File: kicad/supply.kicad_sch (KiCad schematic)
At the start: 36 parts, among them J5 Screw_Terminal_01x03, SW1 SW_DPDT_x2, SW2 SW_DPDT_x2, SW3 SW_DPDT_x2, SW5 SW_DPDT_x2, U6 LM2937-5, U9 LM317_TO-252

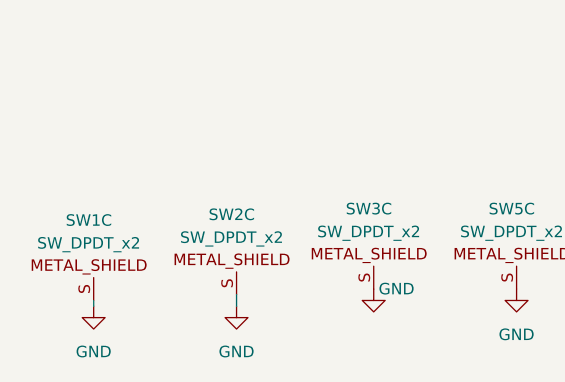
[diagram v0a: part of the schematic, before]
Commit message: Updated Schematic, removed sw1,2,3a,4, have to fix 3a for zero offset switch
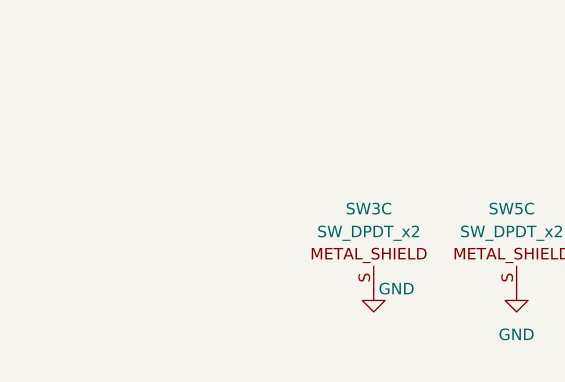
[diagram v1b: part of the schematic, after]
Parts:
- removed SW1, SW2: SW_DPDT_x2, lib:MHS222, symbol local_lib:SW_DPDT_x2

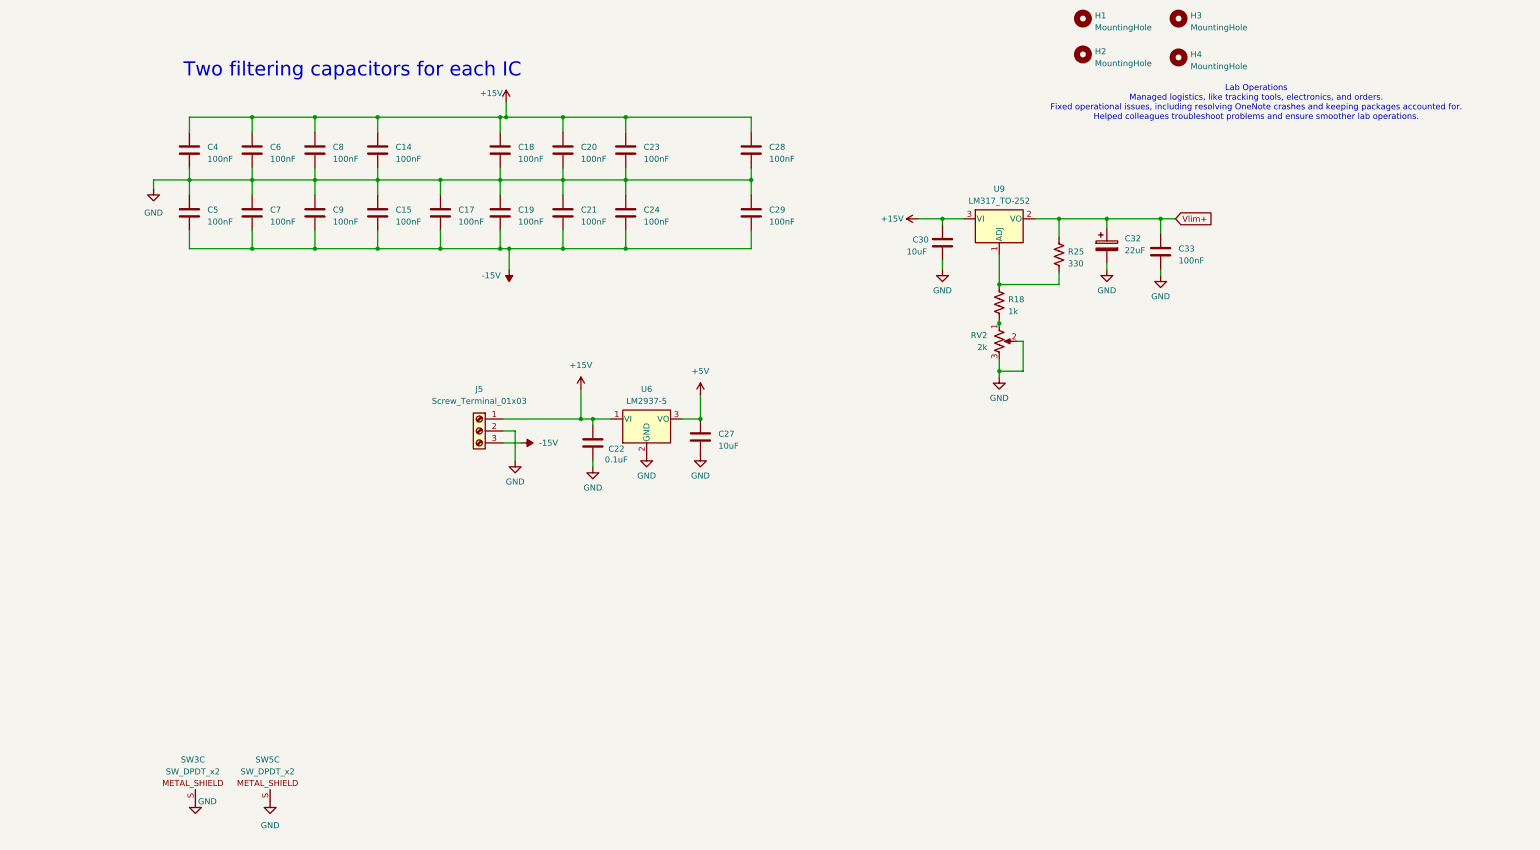
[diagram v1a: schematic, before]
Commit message: Finished Cleaning up Schematic, TODO: Add LED and pick parts
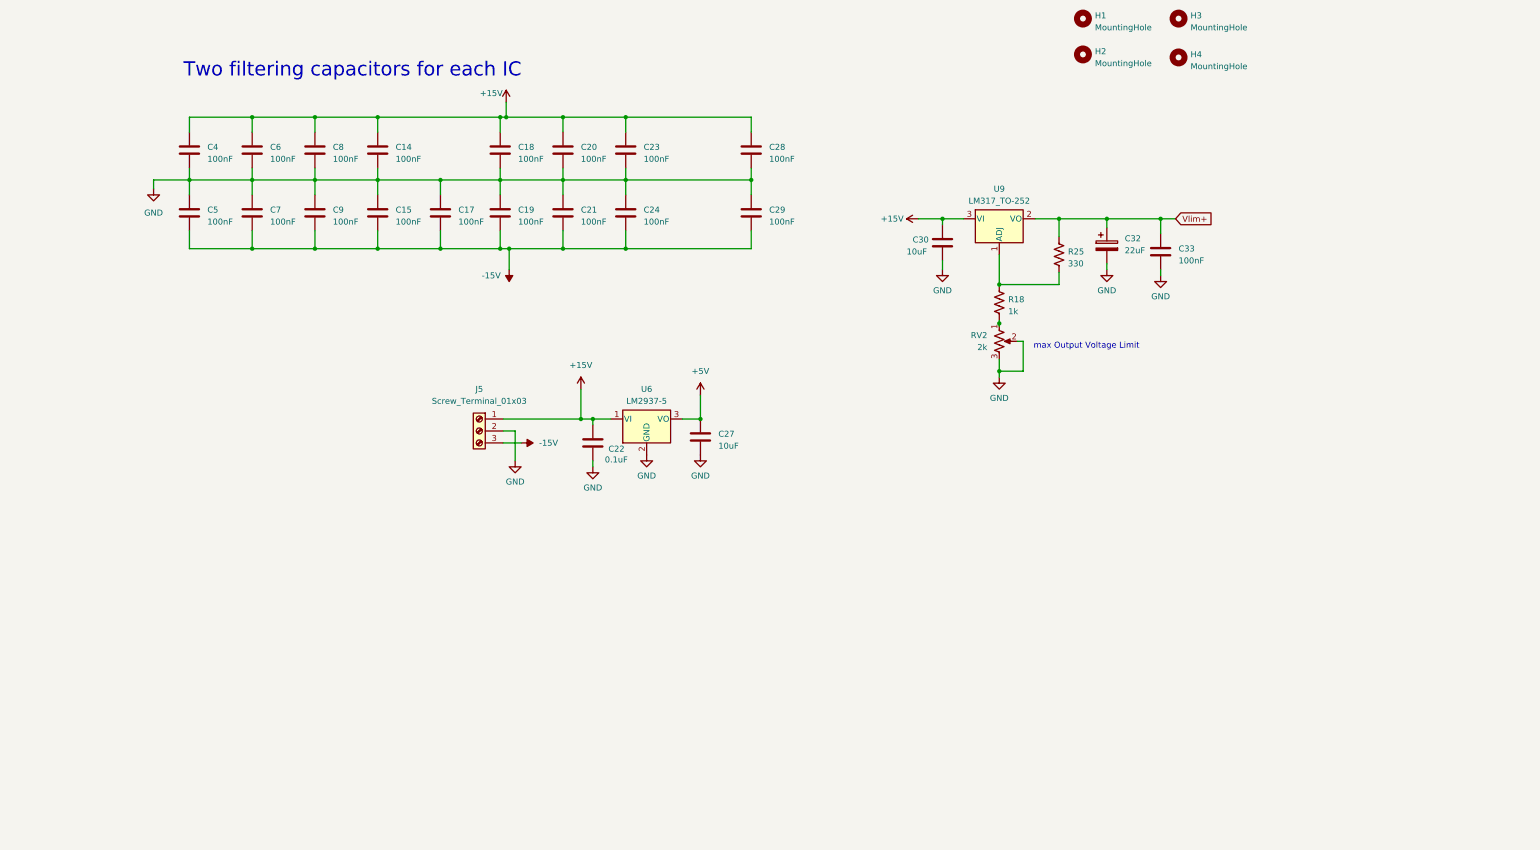
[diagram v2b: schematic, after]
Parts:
- removed SW3, SW5: SW_DPDT_x2, lib:MHS222, symbol local_lib:SW_DPDT_x2
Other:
- note added: "max Output Voltage Limit"
- note removed: "Lab Operations Managed logistics, like tracking tools, electronics, and orders. Fixed operational issues, including resolving OneNote crashes and keeping packages accounted for. Helped colleagues troubleshoot problems and ensure smoother lab operations."

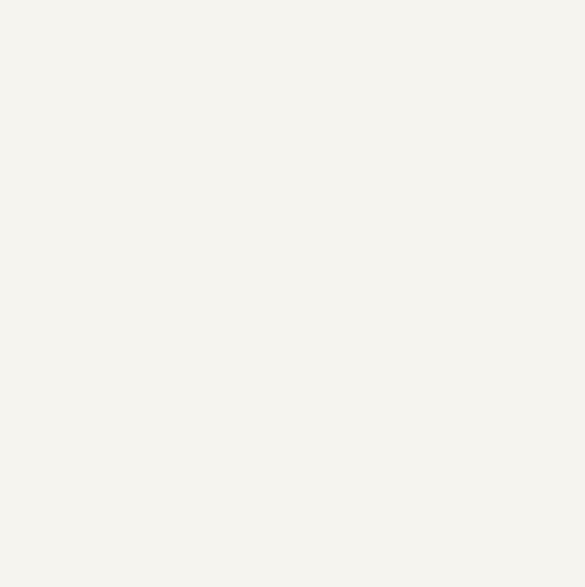
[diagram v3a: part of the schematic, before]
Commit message: Added all features to schematic, TODO: fix pot footprint and layout pcb
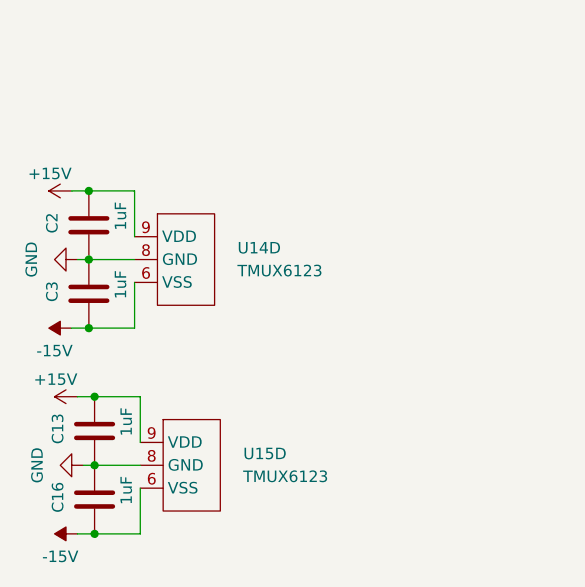
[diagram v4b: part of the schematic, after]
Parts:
- added C13, C16, C2, C3: 1uF, Capacitor_SMD:C_0805_2012Metric, symbol Device:C
- added U14, U15: TMUX6123, Package_SO:VSSOP-10_3x3mm_P0.5mm, symbol library_intensity_pi:TMUX6123_split
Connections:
- net +15V: now also C13.1, C2.1, U14.9 (VDD), U15.9 (VDD)
- net -15V: now also C16.2, C3.2, U14.6 (VSS), U15.6 (VSS)
- net GND: now also C13.2, C16.1, C2.2, C3.1, U14.8 (GND), U15.8 (GND)

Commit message: First portion of routing
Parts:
- added C26, C31, C34, C35, C36, C37, C38, C39, C40, C42: 100nF, Capacitor_SMD:C_0805_2012Metric, symbol Device:C
- renumbered U15 to U17
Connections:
- net +15V: now also C26.1, C34.1, C36.1, C38.1, C40.1
- net -15V: now also C31.2, C35.2, C37.2, C39.2, C42.2
- net GND: now also C26.2, C31.1, C34.2, C35.1, C36.2, C37.1, C38.2, C39.1, C40.2, C42.1
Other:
- moved on the sheet: C14, C15, C17, C18, C19, C20, C21, C23, C24, C28, C29, C30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

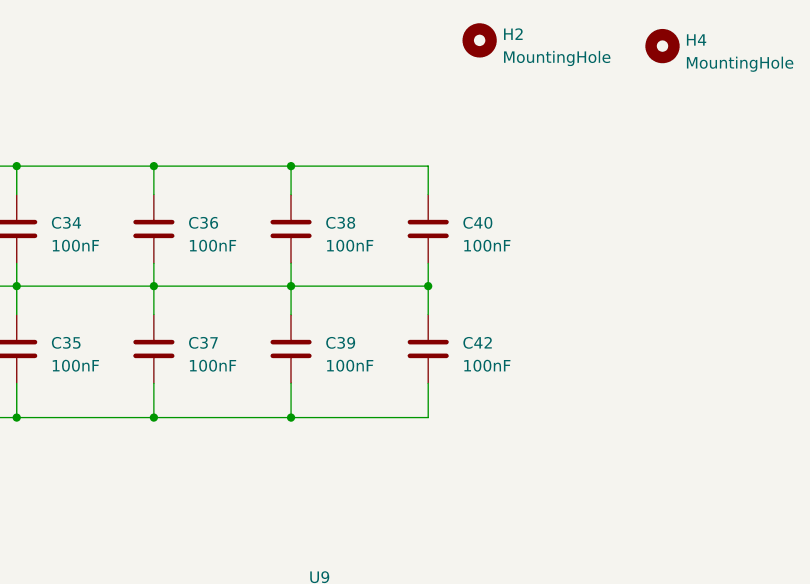
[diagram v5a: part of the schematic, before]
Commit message: Updates to PCB placement, removed one extra capacitor pair
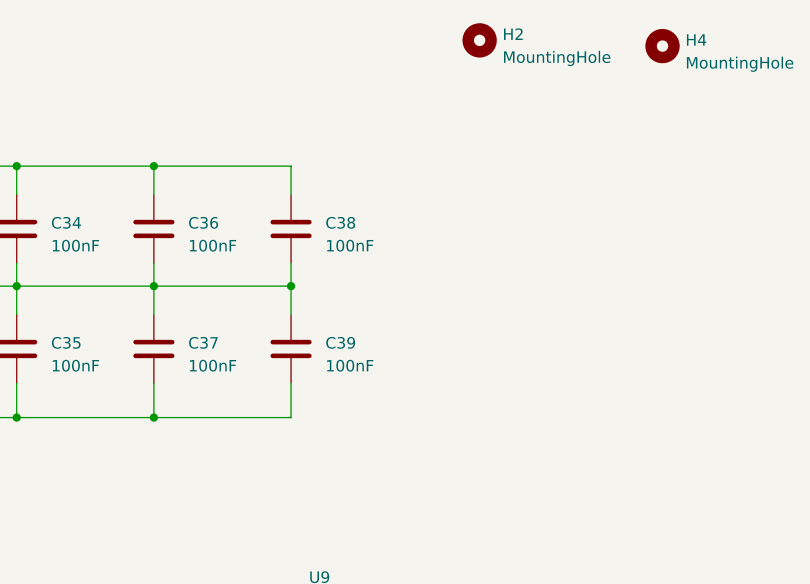
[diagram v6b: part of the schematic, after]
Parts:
- removed C40, C42: 100nF, Capacitor_SMD:C_0805_2012Metric, symbol Device:C
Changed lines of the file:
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@@
 	)
 	(junction
-		(at 238.125 51.435)
-		(diameter 0)
-		(color 0 0 0 0)
-	)
-	(junction
 		(at 118.11 51.435)
 		(diameter 0)
@@
 	)
 	(junction
-		(at 222.885 38.1)
-		(diameter 0)
-		(color 0 0 0 0)
-	)
-	(junction
 		(at 144.78 66.04)
 		(diameter 0)
@@
 	)
 	(junction
-		(at 222.885 66.04)
-		(diameter 0)
-		(color 0 0 0 0)
-	)
-	(junction
 		(at 139.7 101.6)
 		(diameter 0)
@@
 	(wire
 		(pts
-			(xy 238.125 62.23) (xy 238.125 66.04)
-		)
-		(stroke
-			(width 0)
-			(type default)
-		)
-	)
-	(wire
-		(pts
 			(xy 92.075 38.1) (xy 118.11 38.1)
 		)
@@
 	(wire
 		(pts
-			(xy 238.125 48.895) (xy 238.125 51.435)
-		)
-		(stroke
-			(width 0)
-			(type default)
-		)
-	)
-	(wire
-		(pts
 			(xy 52.07 66.04) (xy 65.405 66.04)
 		)
@@
 	(wire
 		(pts
-			(xy 222.885 38.1) (xy 238.125 38.1)
-		)
-		(stroke
-			(width 0)
-			(type default)
-		)
-	)
-	(wire
-		(pts
 			(xy 44.45 52.705) (xy 46.355 52.705)
 		)
@@
 	(wire
 		(pts
-			(xy 222.885 66.04) (xy 238.125 66.04)
-		)
-		(stroke
-			(width 0)
-			(type default)
-		)
-	)
-	(wire
-		(pts
 			(xy 53.975 130.81) (xy 48.895 130.81)
 		)
@@
 	(wire
 		(pts
-			(xy 238.125 51.435) (xy 238.125 54.61)
-		)
-		(stroke
-			(width 0)
-			(type default)
-		)
-	)
-	(wire
-		(pts
 			(xy 213.995 90.17) (xy 213.995 91.44)
 		)
@@
 	(wire
 		(pts
-			(xy 238.125 38.1) (xy 238.125 41.275)
-		)
-		(stroke
-			(width 0)
-			(type default)
-		)
-	)
-	(wire
-		(pts
 			(xy 44.45 51.435) (xy 44.45 52.705)
 		)
@@
 		)
 	)
-	(wire
-		(pts
-			(xy 222.885 51.435) (xy 238.125 51.435)
-		)
-		(stroke
-			(width 0)
-			(type default)
-		)
-	)
 	(global_label "Vlim+"
 		(shape input)
@@
 	(symbol
 		(lib_id "Device:C")
-		(at 238.125 45.085 0)
-		(unit 1)
-		(exclude_from_sim no)
-		(in_bom yes)
-		(on_board yes)
-		(dnp no)
-		(fields_autoplaced yes)
-		(property "Reference" "C40"
-			(at 241.935 44.45 0)
-			(effects
-				(font
-					(size 1.27 1.27)
-				)
-				(justify left)
-			)
-		)
-		(property "Value" "100nF"
-			(at 241.935 46.99 0)
-			(effects
-				(font
-					(size 1.27 1.27)
-				)
-				(justify left)
-			)
-		)
-		(property "Footprint" "Capacitor_SMD:C_0805_2012Metric"
-			(at 239.0902 48.895 0)
-			(effects
-				(font
-					(size 1.27 1.27)
-				)
-				(hide yes)
-			)
-		)
-		(property "Datasheet" "~"
-			(at 238.125 45.085 0)
-			(effects
-				(font
-					(size 1.27 1.27)
-				)
-				(hide yes)
-			)
-		)
-		(property "Description" ""
-			(at 238.125 45.085 0)
-			(effects
-				(font
-					(size 1.27 1.27)
-				)
-				(hide yes)
-			)
-		)
-		(pin "1"
-		)
-		(pin "2"
-		)
-		(instances
-			(project "intensity_pi"
-				(path "/3a3d7bcb-6fa5-41ef-9ea1-6d4ab7c492fd/a04c5785-e230-4149-bf27-97ee4701c201"
-					(reference "C40")
-					(unit 1)
-				)
-			)
-		)
-	)
-	(symbol
-		(lib_id "Device:C")
 		(at 160.655 58.42 0)
 		(unit 1)
@@
 					(unit 1)
 				)
-			)
-		)
-	)
-	(symbol
-		(lib_id "Device:C")
-		(at 238.125 58.42 0)
-		(unit 1)
-		(exclude_from_sim no)
-		(in_bom yes)
-		(on_board yes)
-		(dnp no)
-		(fields_autoplaced yes)
-		(property "Reference" "C42"
-			(at 241.935 57.785 0)
-			(effects
-				(font
-					(size 1.27 1.27)
-				)
-				(justify left)
-			)
-		)
-		(property "Value" "100nF"
-			(at 241.935 60.325 0)
-			(effects
-				(font
-					(size 1.27 1.27)
-				)
-				(justify left)
-			)
-		)
-		(property "Footprint" "Capacitor_SMD:C_0805_2012Metric"
-			(at 239.0902 62.23 0)
-			(effects
-				(font
-					(size 1.27 1.27)
-				)
-				(hide yes)
-			)
-		)
-		(property "Datasheet" "~"
-			(at 238.125 58.42 0)
-			(effects
-				(font
-					(size 1.27 1.27)
-				)
-				(hide yes)
-			)
-		)
-		(property "Description" ""
-			(at 238.125 58.42 0)
-			(effects
-				(font
-					(size 1.27 1.27)
-				)
-				(hide yes)
-			)
-		)
-		(pin "1"
-		)
-		(pin "2"
-		)
-		(instances
-			(project "intensity_pi"
-				(path "/3a3d7bcb-6fa5-41ef-9ea1-6d4ab7c492fd/a04c5785-e230-4149-bf27-97ee4701c201"
-					(reference "C42")
-					(unit 1)
-				)

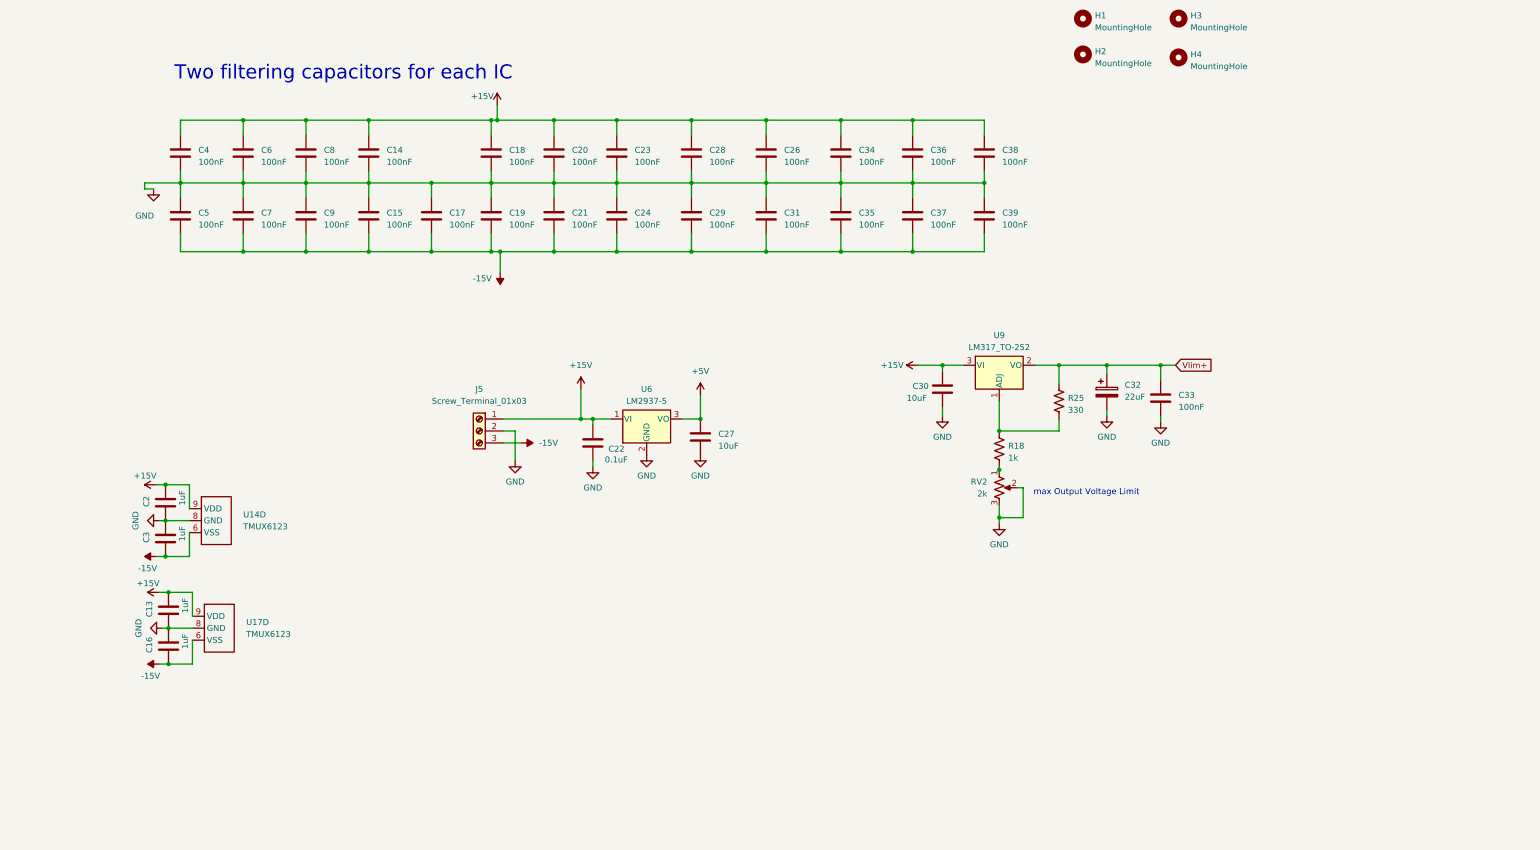
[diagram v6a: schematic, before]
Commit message: Fixed Error Threshold Control, replaced 2x optocouplers with transistors, added power rectification + regulators for 15VAC to +- 15VDC, finished pcb routing, TODO: Check all components have parts, check IC cap filtering, check error threshold schem
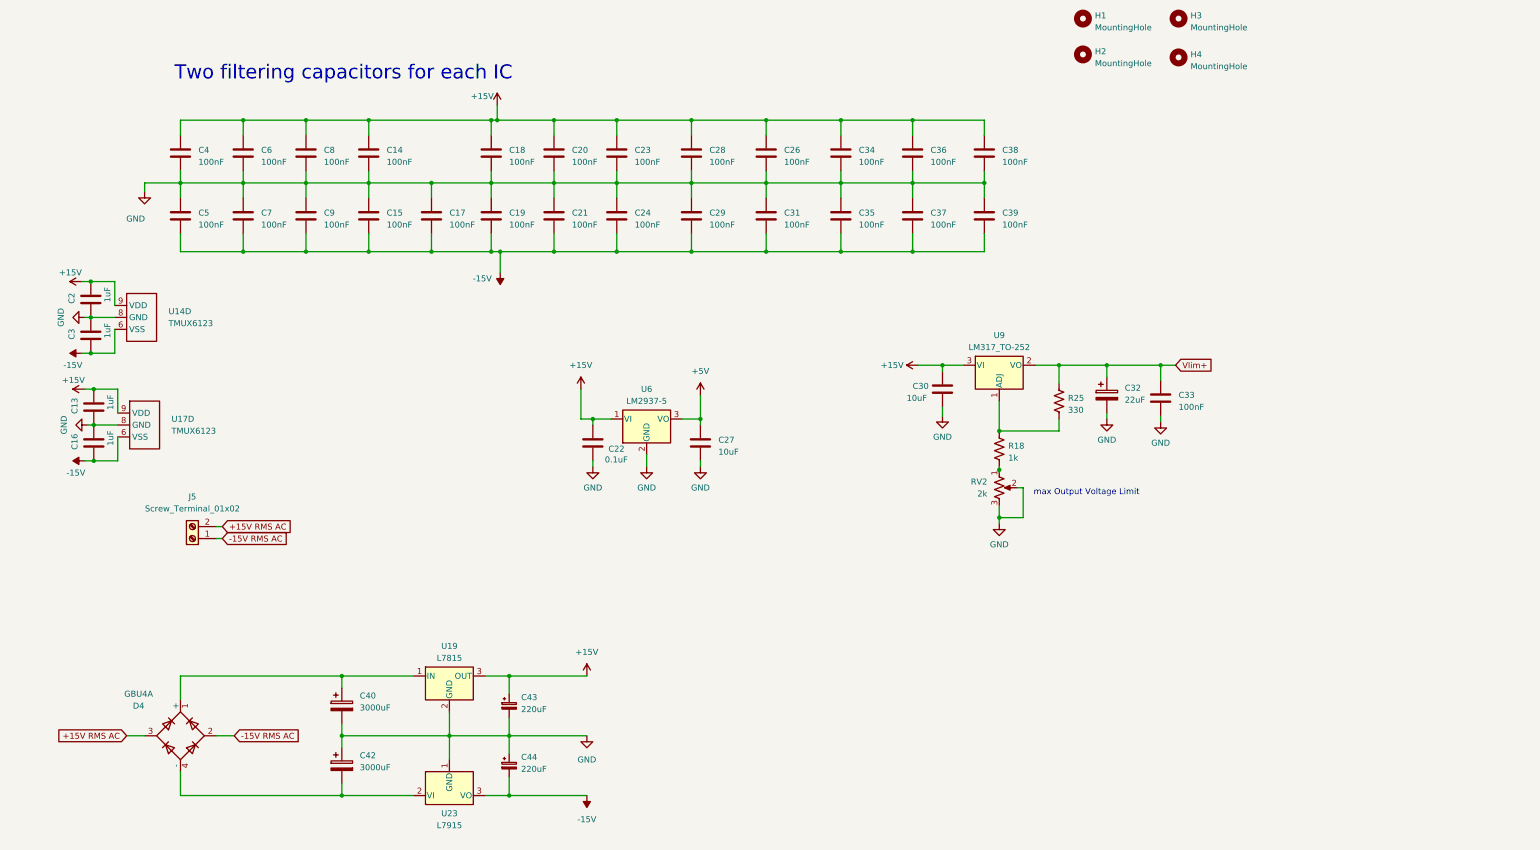
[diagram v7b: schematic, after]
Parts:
- removed J5: Screw_Terminal_01x03, TerminalBlock_4Ucon:TerminalBlock_4Ucon_1x03_P3.50mm_Horizontal, symbol Connector:Screw_Terminal_01x03
- added C40, C42: 3000uF, Capacitor_SMD:CP_Elec_18x22, symbol Device:C_Polarized
- added C43, C44: 220uF, Capacitor_SMD:CP_Elec_10x10.5, symbol Device:C_Polarized_Small
- added D4: GBU4A, Diode_THT:Diode_Bridge_Vishay_GBU, symbol Diode_Bridge:GBU4A
- added J5: Screw_Terminal_01x02, TerminalBlock_4Ucon:TerminalBlock_4Ucon_1x02_P3.50mm_Horizontal, symbol Connector:Screw_Terminal_01x02
- added U19: L7815, Package_TO_SOT_SMD:TO-252-3_TabPin2, symbol Regulator_Linear:L7815
- added U23: L7915, Package_TO_SOT_SMD:TO-252-3_TabPin2, symbol Regulator_Linear:L7915
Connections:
- net +15V: now also C43.1, U19.3 (OUT)
- net -15V: now also C44.2, U23.3 (VO)
- net GND: now also C40.2, C42.1, C43.2, C44.1, U19.2 (GND), U23.1 (GND)
- new net: C40.1, D4.1 (+), U19.1 (IN)
- new net: C42.2, D4.4 (-), U23.2 (VI)
- new net +15V RMS AC: D4.3, J5.2 (Pin_2)
- new net -15V RMS AC: D4.2, J5.1 (Pin_1)
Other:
- moved on the sheet: C13, C16, C2, C27, C3, C32, U14D, U17D
